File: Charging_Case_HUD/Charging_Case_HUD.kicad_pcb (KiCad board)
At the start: 2 copper layers, 152.5 x 64.6 mm, 140 parts, among them IC1 LM5155DSSR, J1 Conn_01x20, J2 09551296822741, J3 Conn_01x02, J4 Conn_01x02, J5 Conn_01x02, J6 Conn_01x02, J7 Conn_01x02, J8 SWD, Q1 CSD18537NQ5A, SW1 SW_MEC_5G, SW2 SW_DIP_x01, SW3 SW_SPDT, U1 ILI9163C, U2 STM32F105RCTx, U3 SN65HVD230, U4 SN65HVD230, U5 LMR51420, U6 AMS1117-3.3, Y1 16MHz

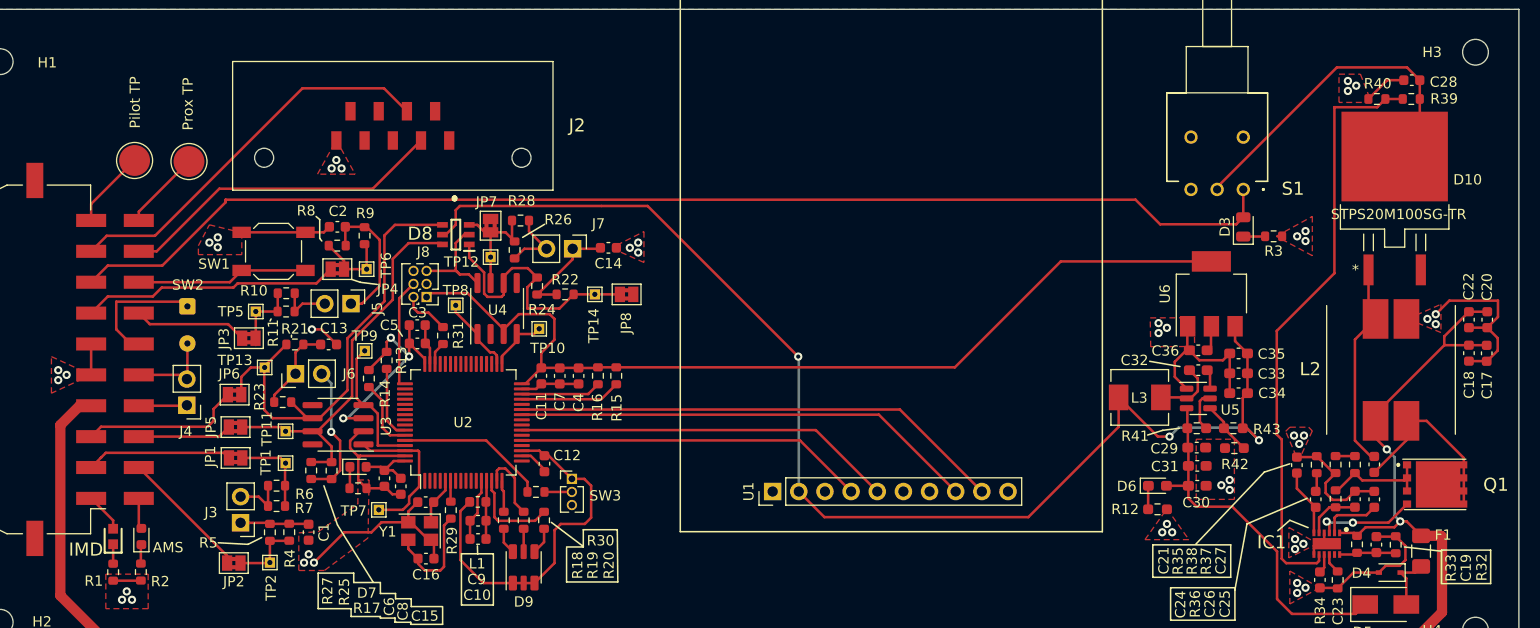
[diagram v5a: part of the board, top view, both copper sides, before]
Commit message: updated connector
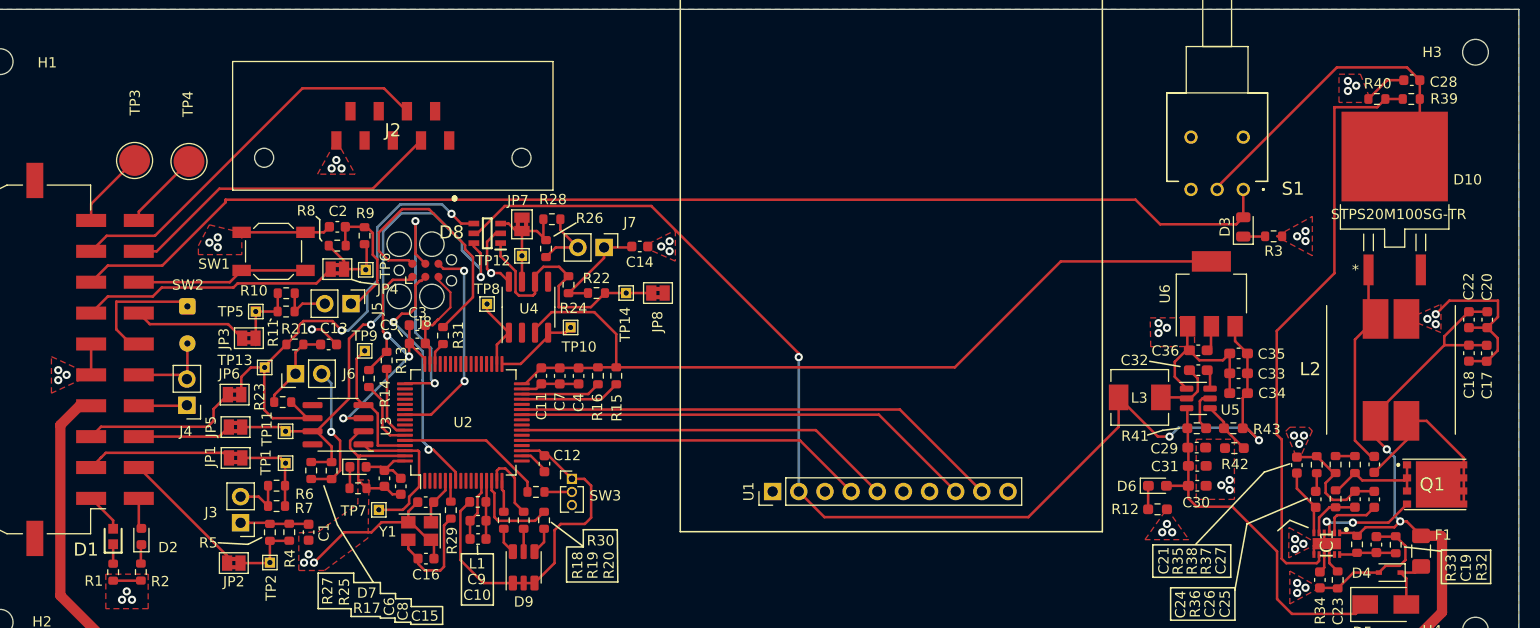
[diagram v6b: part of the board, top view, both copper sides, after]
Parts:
- J8: footprint Connector_PinHeader_1.27mm:PinHeader_2x03_P1.27mm_Vertical -> Connector:Tag-Connect_TC2030-IDC-FP_2x03_P1.27mm_Vertical
- TP3: renamed from Pilot TP
- TP4: renamed from Prox TP
- moved JP8 3.05 mm to (114.6, 55.8)
- moved R22 3.05 mm to (108.7, 55.8)
- moved TP12 3.05 mm to (101.4, 52.1)
- moved TP14 3.05 mm to (111.6, 55.8)
- moved TP8 3.05 mm to (98.0, 56.8)
- moved C14 3.05 mm to (112.9, 51.2)
- moved D8 3.05 mm to (98.1, 50.0)
- moved J7 3.05 mm to (109.4, 51.3)
- moved JP7 3.05 mm to (101.4, 49.1)
- moved R24 3.05 mm to (106.0, 54.9)
- moved R26 3.05 mm to (103.8, 51.4)
- moved R28 3.05 mm to (104.3, 48.6)
- moved TP10 3.05 mm to (106.2, 59.1)
- moved U4 3.05 mm to (102.1, 57.1)
- moved J8 2.60 mm to (92.0, 53.5), turned to 0 degrees
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- renumbered IMD to D1, AMS to D2
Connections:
- J8 pad 3: unconnected-(J8-Pad3) -> /MCU2/NRST
- J8 pad 6: unconnected-(J8-Pad6) -> /MCU2/PB3
- U2 pad 7: unconnected-(U2-Pad7) -> /MCU2/NRST
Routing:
- net /MCU2/NRST: track 0.00 -> 24.4 mm, vias 0 -> 2
- net Net-(J8-Pad2): track 4.71 -> 25.8 mm
- net /MCU2/PB3: track 0.00 -> 20.8 mm, vias 0 -> 2
- net Net-(D8-Pad6): track 38.4 -> 52.8 mm, vias 0 -> 2
- net /MCU2/SWCLK: track 10.1 -> 24.0 mm, vias 0 -> 2
- net +5V: track 123.1 -> 119.3 mm
- net CAN_Shield: track 147.3 -> 150.9 mm, vias 46 -> 47
- net Net-(D8-Pad4): track 46.5 -> 49.3 mm, vias 0 -> 2
- net /MCU2/CAN2_RX: track 5.90 -> 8.35 mm
- net Net-(C2-Pad2): track 13.7 -> 13.2 mm
